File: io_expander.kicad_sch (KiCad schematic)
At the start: 8 parts, among them J2 UPDI, U8 ATtiny427

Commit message: WIP: display
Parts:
- renumbered U8 to U9
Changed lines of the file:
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@@
   (symbol (lib_id "MCU_Microchip_ATtiny:ATtiny417-M") (at 88.9 88.9 0) (unit 1)
     (in_bom yes) (on_board yes)
-    (property "Reference" "U8" (id 0) (at 93.98 59.69 0)
+    (property "Reference" "U9" (id 0) (at 93.98 59.69 0)
       (effects (font (size 1.27 1.27)) (justify left))
     )

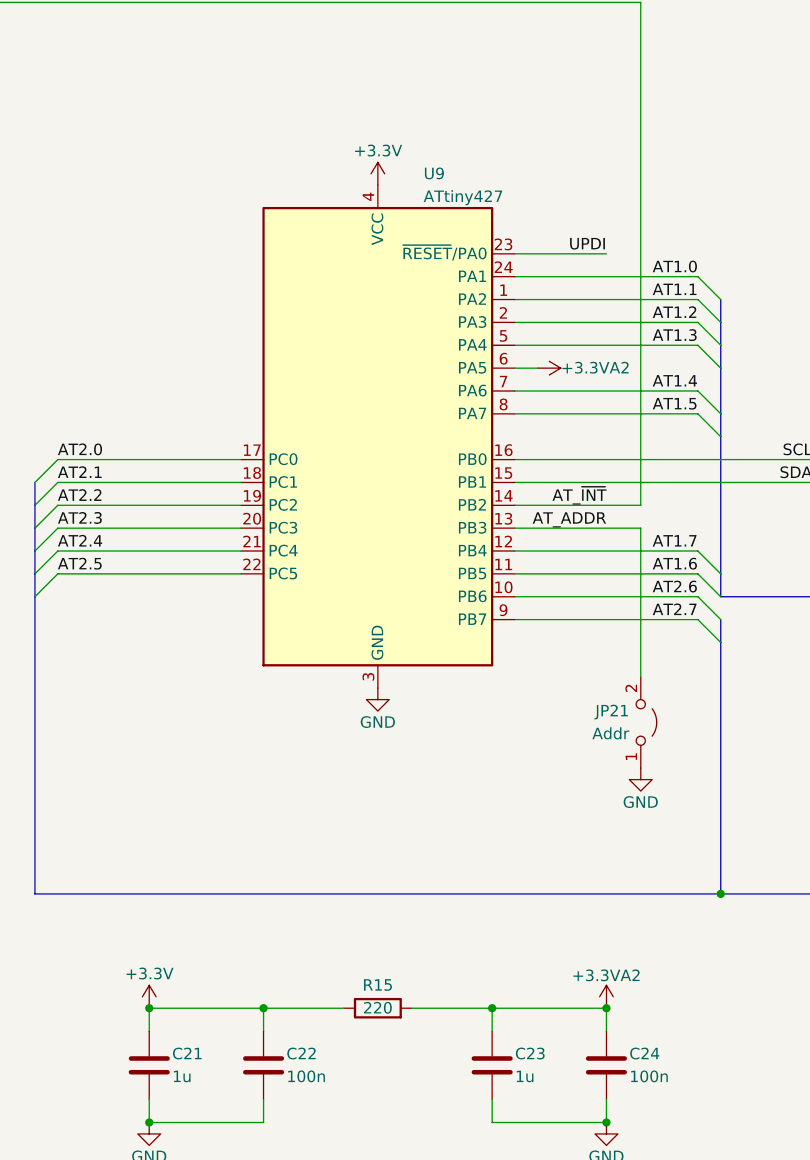
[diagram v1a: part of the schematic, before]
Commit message: rev1.1: Add I2C pullups
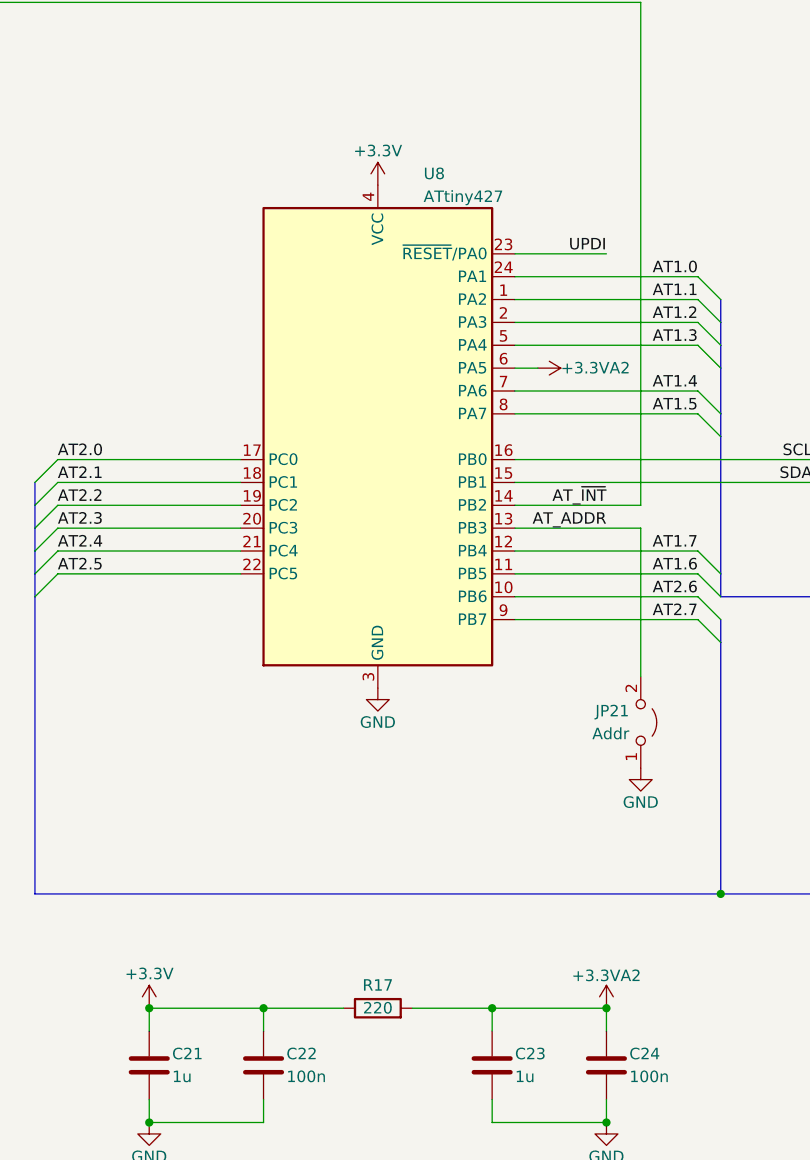
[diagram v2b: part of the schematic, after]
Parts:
- renumbered R15 to R17, U9 to U8
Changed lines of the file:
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@@
   (title_block
     (title "[canbrd] CAN/RS485 IO board")
-    (date "2022-02-24")
-    (rev "1.0")
+    (date "2022-03-18")
+    (rev "1.1")
   )
   (junction (at 63.5 165.1) (diameter 0) (color 0 0 0 0)
@@
   (symbol (lib_id "power:GND") (at 171.45 73.66 0) (unit 1)
     (in_bom yes) (on_board yes)
-    (property "Reference" "#PWR073" (id 0) (at 171.45 80.01 0)
+    (property "Reference" "#PWR075" (id 0) (at 171.45 80.01 0)
       (effects (font (size 1.27 1.27)) hide)
     )
@@
   (symbol (lib_id "power:GND") (at 88.9 116.84 0) (unit 1)
     (in_bom yes) (on_board yes)
-    (property "Reference" "#PWR075" (id 0) (at 88.9 123.19 0)
+    (property "Reference" "#PWR077" (id 0) (at 88.9 123.19 0)
       (effects (font (size 1.27 1.27)) hide)
     )
@@
   (symbol (lib_id "power_symbols:+3.3VA2") (at 106.68 81.28 270) (unit 1)
     (in_bom yes) (on_board yes)
-    (property "Reference" "#PWR074" (id 0) (at 102.87 81.28 0)
+    (property "Reference" "#PWR076" (id 0) (at 102.87 81.28 0)
       (effects (font (size 1.27 1.27)) hide)
     )
@@
   (symbol (lib_id "power:+3.3V") (at 171.45 68.58 0) (unit 1)
     (in_bom yes) (on_board yes)
-    (property "Reference" "#PWR072" (id 0) (at 171.45 72.39 0)
+    (property "Reference" "#PWR074" (id 0) (at 171.45 72.39 0)
       (effects (font (size 1.27 1.27)) hide)
     )
@@
   (symbol (lib_id "power:GND") (at 114.3 165.1 0) (unit 1)
     (in_bom yes) (on_board yes)
-    (property "Reference" "#PWR080" (id 0) (at 114.3 171.45 0)
+    (property "Reference" "#PWR082" (id 0) (at 114.3 171.45 0)
       (effects (font (size 1.27 1.27)) hide)
     )
@@
   (symbol (lib_id "power:GND") (at 63.5 165.1 0) (unit 1)
     (in_bom yes) (on_board yes)
-    (property "Reference" "#PWR079" (id 0) (at 63.5 171.45 0)
+    (property "Reference" "#PWR081" (id 0) (at 63.5 171.45 0)
       (effects (font (size 1.27 1.27)) hide)
     )
@@
   (symbol (lib_id "power_symbols:+3.3VA2") (at 114.3 152.4 0) (unit 1)
     (in_bom yes) (on_board yes)
-    (property "Reference" "#PWR078" (id 0) (at 114.3 156.21 0)
+    (property "Reference" "#PWR080" (id 0) (at 114.3 156.21 0)
       (effects (font (size 1.27 1.27)) hide)
     )
@@
   (symbol (lib_id "power:GND") (at 118.11 125.73 0) (mirror y) (unit 1)
     (in_bom yes) (on_board yes)
-    (property "Reference" "#PWR076" (id 0) (at 118.11 132.08 0)
+    (property "Reference" "#PWR078" (id 0) (at 118.11 132.08 0)
       (effects (font (size 1.27 1.27)) hide)
     )
@@
   (symbol (lib_id "power:+3.3V") (at 88.9 60.96 0) (unit 1)
     (in_bom yes) (on_board yes)
-    (property "Reference" "#PWR071" (id 0) (at 88.9 64.77 0)
+    (property "Reference" "#PWR073" (id 0) (at 88.9 64.77 0)
       (effects (font (size 1.27 1.27)) hide)
     )
@@
   (symbol (lib_id "Device:R") (at 88.9 152.4 90) (unit 1)
     (in_bom yes) (on_board yes)
-    (property "Reference" "R15" (id 0) (at 88.9 149.86 90))
+    (property "Reference" "R17" (id 0) (at 88.9 149.86 90))
     (property "Value" "220" (id 1) (at 88.9 152.4 90))
     (property "Footprint" "Resistor_SMD:R_0603_1608Metric" (id 2) (at 88.9 154.178 90)
@@
   (symbol (lib_id "power:+3.3V") (at 63.5 152.4 0) (unit 1)
     (in_bom yes) (on_board yes)
-    (property "Reference" "#PWR077" (id 0) (at 63.5 156.21 0)
+    (property "Reference" "#PWR079" (id 0) (at 63.5 156.21 0)
       (effects (font (size 1.27 1.27)) hide)
     )
@@
   (symbol (lib_id "MCU_Microchip_ATtiny:ATtiny417-M") (at 88.9 88.9 0) (unit 1)
     (in_bom yes) (on_board yes)
-    (property "Reference" "U9" (id 0) (at 93.98 59.69 0)
-      (effects (font (size 1.27 1.27)) (justify left))
-    )
+    (property "Reference" "U8" (id 0) (at 93.98 59.69 0)
+      (effects (font (size 1.27 1.27)) (justify left))
+    )

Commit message: lots changed
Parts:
- removed C22, C24: 100n, Capacitor_SMD:C_0603_1608Metric, symbol Device:C
- removed C23: 1u, Capacitor_SMD:C_0603_1608Metric, symbol Device:C
- removed J2: UPDI, Connector_PinHeader_1.27mm:PinHeader_2x03_P1.27mm_Vertical_SMD, symbol Connector_Generic:Conn_02x03_Odd_Even
- removed JP21: Addr, Jumper:SolderJumper-2_P1.3mm_Open_TrianglePad1.0x1.5mm, symbol Jumper:Jumper_2_Open
- removed R17: 220, Resistor_SMD:R_0603_1608Metric, symbol Device:R
- removed U8: ATtiny427, Package_DFN_QFN:QFN-24-1EP_4x4mm_P0.5mm_EP2.6x2.6mm, symbol MCU_Microchip_ATtiny:ATtiny417-M
- added D19: 33V, Diode_SMD:D_SMB, symbol Device:D_TVS
- added F1, F2, F3, F4, F5, F6, F7: 500mA, Fuse:Fuse_1206_3216Metric, symbol Device:Fuse_Small
- added JP9: Jumper_2_Open, Jumper:SolderJumper-2_P1.3mm_Open_TrianglePad1.0x1.5mm, symbol Jumper:Jumper_2_Open
- added U7: 74HC595, Package_SO:SOIC-16_3.9x9.9mm_P1.27mm, symbol 74xx:74HC595
- added U8: ULN2003A, Package_SO:SOIC-16_3.9x9.9mm_P1.27mm, symbol Transistor_Array:ULN2003A
- C21: value 1u -> 100n
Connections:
- net +3V3: now also U7.10 (~{SRCLR}), U7.16 (VCC)
- net GND: now also D19.2 (A2), U7.13 (~{OE}), U7.8 (GND), U8.8 (GND)
- new net: JP9.1 (A), U7.7 (QH)
- new net: F4.1, U8.13 (O4)
- new net: U7.1 (QB), U8.6 (I6)
- new net: U7.15 (QA), U8.7 (I7)
- new net: U7.2 (QC), U8.5 (I5)
- new net: U7.3 (QD), U8.4 (I4)
- new net: U7.4 (QE), U8.3 (I3)
- new net: U7.5 (QF), U8.2 (I2)
- new net: U7.6 (QG), U8.1 (I1)
- new net: F2.1, U8.11 (O6)
- new net: F1.1, U8.10 (O7)
- new net: F7.1, U8.16 (O1)
- new net: F3.1, U8.12 (O5)
- new net: F5.1, U8.14 (O3)
- new net: F6.1, U8.15 (O2)
- new net 595_~{CS}: U7.12 (RCLK)
- new net MOSI: U7.14 (SER)
- new net OUT0: F1.2
- new net OUT1: F2.2
- new net OUT2: F3.2
- new net OUT3: F4.2
- new net OUT4: F5.2
- new net OUT5: F6.2
- new net OUT6: F7.2
- new net OUT7: JP9.2 (B)
- new net O_TVS: D19.1 (A1), U8.9 (COM)
- new net SCK: U7.11 (SRCLK)
- no-connect marks 3 -> 1
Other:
- removed sheet IO Expander Power IO
- removed sheet IO Expander Protection

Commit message: things changed
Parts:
- renumbered C21 to C33, D19 to D18, JP9 to JP5, U7 to U8, U8 to U9
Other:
- moved on the sheet: C33, D18, F1, F2, F3, F4, F5, F6, F7, JP5, U8, U9

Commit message: isolate and other stuff
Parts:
- removed JP5: Jumper_2_Open, Jumper:SolderJumper-2_P1.3mm_Open_TrianglePad1.0x1.5mm, symbol Jumper:Jumper_2_Open
- added D18: D, Diode_SMD:D_SMB, symbol Device:D
- added D19: 60v, Diode_SMD:D_SMB, symbol Device:D_TVS
- added F8: 2A, Littelfuse-154:Littelfuse-154-2920, symbol Device:Fuse
- added Q20: AO4266E, Package_SO:SOIC-8_3.9x4.9mm_P1.27mm, symbol Transistor_FET:FDS9435A
- added R51: 10k, Resistor_SMD:R_0603_1608Metric, symbol Device:R
- renumbered C33 to C32, D18 to D20, U8 to U7, U9 to U8
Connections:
- net GND: now also D20.1 (A1), D18.2 (A), D19.1 (A1), Q20.1 (S), Q20.2 (S), Q20.3 (S), R51.2; no longer D20.2 (A2)
- net OUT7: now also D18.1 (K), D19.2 (A2), F8.2
- net at U7.7 (QH): now also Q20.4 (G), R51.1
- net O_TVS renamed VIO2
- net VIO2: now also D20.2 (A2); no longer D20.1 (A1)
- new net xOUT7: F8.1, Q20.5 (D), Q20.6 (D), Q20.7 (D), Q20.8 (D)
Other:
- title: [canbrd] CAN/RS485 IO board -> [canbrd] CAN IO board
- moved on the sheet: D20

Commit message: things changed
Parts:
- D12: renamed from D20; value 33V -> 30V
- F8: footprint Littelfuse-154:Littelfuse-154-2920 -> keystone-3522:Keystone_3522
- renumbered C32 to C18, D18 to D10, D19 to D11, Q20 to Q9, R51 to R36, U7 to U3, U8 to U4
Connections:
- net GND: now also D11.2 (A2); no longer D11.1 (A1)
- net OUT7: no longer D10.1 (K), D11.2 (A2)
- net xOUT7: now also D10.1 (K), D11.1 (A1)
- net +3V3 renamed +3.3V
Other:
- moved on the sheet: D10, D11, F8

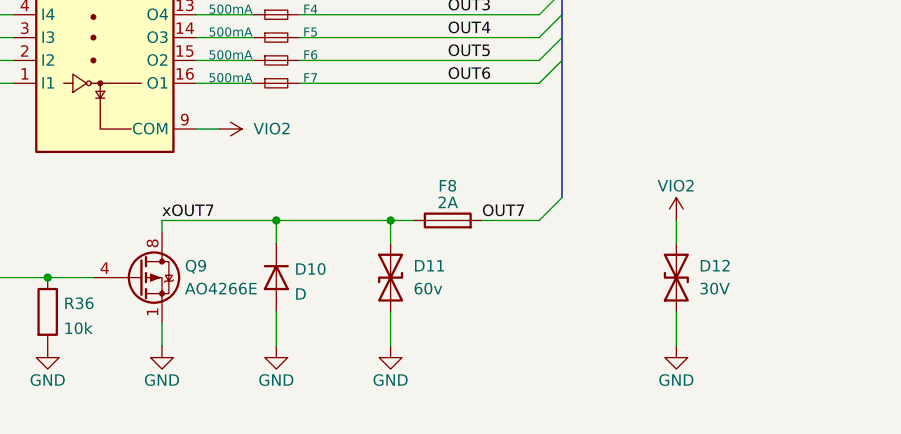
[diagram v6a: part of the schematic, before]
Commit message: Minimal design for testing
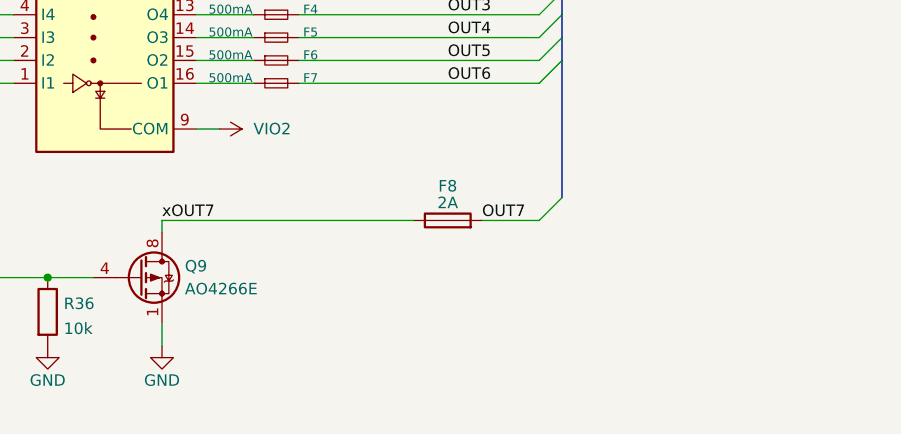
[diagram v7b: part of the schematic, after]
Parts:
- removed D10: D, Diode_SMD:D_SMB, symbol Device:D
- removed D11: 60v, Diode_SMD:D_SMB, symbol Device:D_TVS
- removed D12: 30V, Diode_SMD:D_SMB, symbol Device:D_TVS
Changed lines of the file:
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@@
     (rev "3.2")
-  )
-  (junction (at 171.45 120.65) (diameter 0) (color 0 0 0 0)
-  )
-  (junction (at 184.15 120.65) (diameter 0) (color 0 0 0 0)
   )
   (junction (at 146.05 127) (diameter 0) (color 0 0 0 0)
@@
     (stroke (width 0) (type default) (color 0 0 0 0))
   )
-  (wire (pts (xy 171.45 120.65) (xy 171.45 123.19))
-    (stroke (width 0) (type default) (color 0 0 0 0))
-  )
   (wire (pts (xy 162.56 105.41) (xy 168.91 105.41))
     (stroke (width 0) (type default) (color 0 0 0 0))
@@
     (stroke (width 0) (type default) (color 0 0 0 0))
   )
-  (wire (pts (xy 184.15 120.65) (xy 184.15 123.19))
-    (stroke (width 0) (type default) (color 0 0 0 0))
-  )
   (wire (pts (xy 162.56 95.25) (xy 168.91 95.25))
     (stroke (width 0) (type default) (color 0 0 0 0))
@@
     (stroke (width 0) (type default) (color 0 0 0 0))
   )
-  (wire (pts (xy 215.9 120.65) (xy 215.9 123.19))
-    (stroke (width 0) (type default) (color 0 0 0 0))
-  )
   (bus (pts (xy 50.8 63.5) (xy 76.2 63.5))
     (stroke (width 0) (type default) (color 0 0 0 0))
@@
     (stroke (width 0) (type default) (color 0 0 0 0))
   )
-  (wire (pts (xy 215.9 130.81) (xy 215.9 134.62))
-    (stroke (width 0) (type default) (color 0 0 0 0))
-  )
   (wire (pts (xy 78.74 95.25) (xy 104.14 95.25))
     (stroke (width 0) (type default) (color 0 0 0 0))
   )
-  (wire (pts (xy 171.45 130.81) (xy 171.45 134.62))
-    (stroke (width 0) (type default) (color 0 0 0 0))
-  )
   (wire (pts (xy 124.46 105.41) (xy 142.24 105.41))
     (stroke (width 0) (type default) (color 0 0 0 0))
@@
     (stroke (width 0) (type default) (color 0 0 0 0))
   )
-  (wire (pts (xy 184.15 120.65) (xy 186.69 120.65))
-    (stroke (width 0) (type default) (color 0 0 0 0))
-  )
-  (wire (pts (xy 184.15 130.81) (xy 184.15 134.62))
-    (stroke (width 0) (type default) (color 0 0 0 0))
-  )
   (bus (pts (xy 203.2 90.17) (xy 203.2 92.71))
     (stroke (width 0) (type default) (color 0 0 0 0))
@@
     (stroke (width 0) (type default) (color 0 0 0 0))
   )
-  (wire (pts (xy 158.75 120.65) (xy 171.45 120.65))
-    (stroke (width 0) (type default) (color 0 0 0 0))
-  )
-  (wire (pts (xy 171.45 120.65) (xy 184.15 120.65))
+  (wire (pts (xy 158.75 120.65) (xy 186.69 120.65))
     (stroke (width 0) (type default) (color 0 0 0 0))
   )
@@
     )
     (pin "1")
-  )
-  (symbol (lib_id "Device:D_TVS") (at 184.15 127 90) (mirror x) (unit 1)
-    (in_bom yes) (on_board yes) (fields_autoplaced)
-    (property "Reference" "D11" (id 0) (at 186.69 125.7299 90)
-      (effects (font (size 1.27 1.27)) (justify right))
-    )
-    (property "Value" "60v" (id 1) (at 186.69 128.2699 90)
-      (effects (font (size 1.27 1.27)) (justify right))
-    )
-    (property "Footprint" "Diode_SMD:D_SMB" (id 2) (at 184.15 127 0)
-      (effects (font (size 1.27 1.27)) hide)
-    )
-    (property "Datasheet" "~" (id 3) (at 184.15 127 0)
-      (effects (font (size 1.27 1.27)) hide)
-    )
-    (pin "1")
-    (pin "2")
   )
   (symbol (lib_id "power:+3.3V") (at 76.2 129.54 0) (unit 1)
@@
     (pin "1")
   )
-  (symbol (lib_id "Device:D") (at 171.45 127 270) (unit 1)
-    (in_bom yes) (on_board yes)
-    (property "Reference" "D10" (id 0) (at 173.482 126.0915 90)
-      (effects (font (size 1.27 1.27)) (justify left))
-    )
-    (property "Value" "D" (id 1) (at 173.482 128.8666 90)
-      (effects (font (size 1.27 1.27)) (justify left))
-    )
-    (property "Footprint" "Diode_SMD:D_SMB" (id 2) (at 171.45 127 0)
-      (effects (font (size 1.27 1.27)) hide)
-    )
-    (property "Datasheet" "~" (id 3) (at 171.45 127 0)
-      (effects (font (size 1.27 1.27)) hide)
-    )
-    (pin "1")
-    (pin "2")
-  )
   (symbol (lib_id "power:GND") (at 114.3 118.11 0) (unit 1)
     (in_bom yes) (on_board yes)
@@
     (pin "8")
   )
-  (symbol (lib_id "power_symbols:VIO2") (at 215.9 120.65 0) (unit 1)
-    (in_bom yes) (on_board yes)
-    (property "Reference" "#PWR076" (id 0) (at 215.9 124.46 0)
-      (effects (font (size 1.27 1.27)) hide)
-    )
-    (property "Value" "VIO2" (id 1) (at 215.9 116.84 0))
-    (property "Footprint" "" (id 2) (at 215.9 120.65 0)
-      (effects (font (size 1.27 1.27)) hide)
-    )
-    (property "Datasheet" "" (id 3) (at 215.9 120.65 0)
-      (effects (font (size 1.27 1.27)) hide)
-    )
-    (pin "1")
-  )
   (symbol (lib_id "Device:Fuse_Small") (at 171.45 92.71 0) (unit 1)
     (in_bom yes) (on_board yes)
@@
     (pin "1")
   )
-  (symbol (lib_id "Device:D_TVS") (at 215.9 127 90) (unit 1)
-    (in_bom yes) (on_board yes)
-    (property "Reference" "D12" (id 0) (at 218.44 125.73 90)
-      (effects (font (size 1.27 1.27)) (justify right))
-    )
-    (property "Value" "30V" (id 1) (at 218.44 128.27 90)
-      (effects (font (size 1.27 1.27)) (justify right))
-    )
-    (property "Footprint" "Diode_SMD:D_SMB" (id 2) (at 215.9 127 0)
-      (effects (font (size 1.27 1.27)) hide)
-    )
-    (property "Datasheet" "~" (id 3) (at 215.9 127 0)
-      (effects (font (size 1.27 1.27)) hide)
-    )
-    (pin "1")
-    (pin "2")
-  )
   (symbol (lib_id "Device:Fuse_Small") (at 171.45 95.25 0) (unit 1)
     (in_bom yes) (on_board yes)
@@
     (pin "1")
     (pin "2")
-  )
-  (symbol (lib_id "power:GND") (at 184.15 134.62 0) (unit 1)
-    (in_bom yes) (on_board yes)
-    (property "Reference" "#PWR081" (id 0) (at 184.15 140.97 0)
-      (effects (font (size 1.27 1.27)) hide)
-    )
-    (property "Value" "GND" (id 1) (at 184.15 138.43 0))
-    (property "Footprint" "" (id 2) (at 184.15 134.62 0)
-      (effects (font (size 1.27 1.27)) hide)
-    )
-    (property "Datasheet" "" (id 3) (at 184.15 134.62 0)
-      (effects (font (size 1.27 1.27)) hide)
-    )
-    (pin "1")
   )
   (symbol (lib_id "Device:C") (at 76.2 133.35 0) (unit 1)
@@
     (pin "2")
   )
-  (symbol (lib_id "power:GND") (at 215.9 134.62 0) (unit 1)
-    (in_bom yes) (on_board yes)
-    (property "Reference" "#PWR082" (id 0) (at 215.9 140.97 0)
-      (effects (font (size 1.27 1.27)) hide)
-    )
-    (property "Value" "GND" (id 1) (at 215.9 138.43 0))
-    (property "Footprint" "" (id 2) (at 215.9 134.62 0)
-      (effects (font (size 1.27 1.27)) hide)
-    )
-    (property "Datasheet" "" (id 3) (at 215.9 134.62 0)
-      (effects (font (size 1.27 1.27)) hide)
-    )
-    (pin "1")
-  )
   (symbol (lib_id "Device:Fuse_Small") (at 171.45 100.33 0) (unit 1)
     (in_bom yes) (on_board yes)
@@
     (pin "2")
   )
-  (symbol (lib_id "power:GND") (at 171.45 134.62 0) (unit 1)
-    (in_bom yes) (on_board yes)
-    (property "Reference" "#PWR080" (id 0) (at 171.45 140.97 0)
-      (effects (font (size 1.27 1.27)) hide)
-    )
-    (property "Value" "GND" (id 1) (at 171.45 138.43 0))
-    (property "Footprint" "" (id 2) (at 171.45 134.62 0)
-      (effects (font (size 1.27 1.27)) hide)
-    )
-    (property "Datasheet" "" (id 3) (at 171.45 134.62 0)
-      (effects (font (size 1.27 1.27)) hide)
-    )
-    (pin "1")
-  )
   (symbol (lib_id "power:GND") (at 146.05 134.62 0) (unit 1)
